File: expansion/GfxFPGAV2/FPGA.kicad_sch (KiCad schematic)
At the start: 31 parts, among them J1 JTAG, U1 XC6SLX9-FTG256, U301 XC3S500E-4PQG208I, U302 W25Q64JVSSIM, Y1 ECS-3963

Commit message: More work on VGA card
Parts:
- removed U1: XC6SLX9-FTG256, symbol FPGA_Xilinx_Spartan6:XC6SLX9-FTG256
- removed U301: XC3S500E-4PQG208I, Ddraig:QFP50P3060X3060X409-208N, symbol Ddraig:XC3S500E-4PQG208I
- added U2: XC6SLX9-FTG256, Package_BGA:Xilinx_FTG256, symbol Ddraig:XC6SLX9-FTG256
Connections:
- net +1V2: now also U2.G7 (VCCINT), U2.G9 (VCCINT), U2.H10 (VCCINT), U2.H8 (VCCINT), U2.J7 (VCCINT), U2.J9 (VCCINT), U2.K10 (VCCINT), U2.K8 (VCCINT)
- net +3V3: now also U2.B13 (VCCO_0), U2.B4 (VCCO_0), U2.B9 (VCCO_0), U2.D10 (VCCO_0), U2.D15 (VCCO_1), U2.D2 (VCCO_3), U2.D7 (VCCO_0), U2.E5 (VCCAUX), U2.F11 (VCCAUX), U2.F8 (VCCAUX), U2.G10 (VCCAUX), U2.G13 (VCCO_1), U2.G4 (VCCO_3), U2.H6 (VCCAUX), U2.J10 (VCCAUX), U2.J15 (VCCO_1), U2.J2 (VCCO_3), U2.K13 (VCCO_1), U2.K4 (VCCO_3), U2.L6 (VCCAUX), U2.L9 (VCCAUX), U2.N10 (VCCO_2), U2.N15 (VCCO_1), U2.N2 (VCCO_3), U2.N7 (VCCO_2), U2.R13 (VCCO_1), U2.R4 (VCCO_2), U2.R8 (VCCO_2)
- net FPGA_DONE: now also U2.P13 (DONE_2)
- net FPGA_PROGB: now also U2.T2 (PROGRAM_B_2)
- net GND: now also U2.A1 (GND), U2.A16 (GND), U2.B11 (GND), U2.B7 (GND), U2.D13 (GND), U2.D4 (GND), U2.E9 (GND), U2.G15 (GND), U2.G2 (GND), U2.G8 (GND), U2.H12 (GND), U2.H7 (GND), U2.H9 (GND), U2.J5 (GND), U2.J8 (GND), U2.K7 (GND), U2.K9 (GND), U2.L15 (GND), U2.L2 (GND), U2.M8 (GND), U2.N13 (GND), U2.P3 (GND), U2.R10 (GND), U2.R6 (GND), U2.T1 (GND), U2.T16 (GND)
- net R0: now also U2.A14 (IO_L65N_SCP2_0)
- net R1: now also U2.B14 (IO_L65P_SCP3_0)
- net R2: now also U2.B15 (IO_L29P_A23_M1A13_1)
- net R3: now also U2.B16 (IO_L29N_A22_M1A14_1)
- net TMS: now reaches J1.5 (Pin_5)
- net TMS: now also U2.A15 (TMS)
- net TDO: now reaches J1.4 (Pin_4)
- net TDO: now also U2.E14 (TDO)
- net TCK: now reaches J1.2 (Pin_2)
- net TCK: now also U2.C14 (TCK)
- net TDI: now reaches J1.3 (Pin_3)
- net TDI: now also U2.C12 (TDI)
- no-connect marks 18 -> 0
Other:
- moved on the sheet: C1, C301, C302, C303, C304, C305, C306, C307, C308, C309, C310, D1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

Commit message: Pinout done one VGA card
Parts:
- removed R10, R11, R9: 10K, Resistor_SMD:R_0805_2012Metric, symbol Device:R
- removed R3: 390R, Resistor_SMD:R_0805_2012Metric, symbol Device:R
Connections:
- net CLK_25MHZ is gone; now on net CLK_50MHZ: Y1.3 (O/P)
- net A1: now also U2.P9 (IO_L14N_D12_2); no longer R1.1
- net A10: now also U2.P5 (IO_L49N_D4_2)
- net A11: now also U2.R5 (IO_L48P_D7_2)
- net A12: now also U2.T5 (IO_L48N_RDWR_B_VREF_2)
- net A13: now also U2.N5 (IO_L49P_D3_2)
- net A14: now also U2.N4 (IO_L2N_3)
- net A15: now also U2.P4 (IO_L63P_2)
- net A16: now also U2.T4 (IO_L63N_2)
- net A17: now also U2.N3 (IO_L34P_M3UDQS_3)
- net A18: now also U2.M6 (IO_L64P_D8_2)
- net A19: now also U2.M5 (IO_L2P_3)
- net A2: now also U2.N8 (IO_L29N_GCLK2_2)
- net A3: now also U2.P8 (IO_L30P_GCLK1_D13_2)
- net A4: now also U2.T7 (IO_L32N_GCLK28_2)
- net A5: now also U2.R7 (IO_L32P_GCLK29_2)
- net A6: now also U2.P7 (IO_L31P_GCLK31_D14_2)
- net A7: now also U2.T6 (IO_L47N_2)
- net A8: now also U2.P6 (IO_L47P_2)
- net A9: now also U2.N6 (IO_L64N_D9_2)
- net B0: now also U2.H15 (IO_L37P_A7_M1A0_1)
- net B1: now also U2.H16 (IO_L37N_A6_M1A1_1)
- net B2: now also U2.J14 (IO_L43P_GCLK5_M1DQ4_1)
- net B3: now also U2.J16 (IO_L43N_GCLK4_M1DQ5_1)
- net B4: now also U2.K14 (IO_L41N_GCLK8_M1CASN_1)
- net B5: now also U2.K15 (IO_L44P_A3_M1DQ6_1)
- net B6: now also U2.K16 (IO_L44N_A2_M1DQ7_1)
- net B7: now also U2.L14 (IO_L47P_FWE_B_M1DQ0_1)
- net D0: now also U2.N14 (IO_L45P_A1_M1LDQS_1), U2.T14 (IO_L51P_M1DQ12_1)
- net D1: now also U2.R14 (IO_L50P_M1UDQS_1)
- net D10: now also R1.1, U2.N11 (IO_L13P_M1_2)
- net D11: now also U2.M10 (IO_L16N_VREF_2)
- net D12: now also U2.M12 (IO_L2P_CMPCLK_2)
- net D13: now also U2.N9 (IO_L14P_D11_2)
- net D14: now also U2.T9 (IO_L23N_2); no longer U302.2 (DO/IO1)
- net D15: now also U2.R9 (IO_L23P_2); no longer R4.2
- net D2: now also U2.T13 (IO_L51N_M1DQ13_1)
- net D3: now also U2.T12 (IO_L52N_M1DQ15_1)
- net D4: now also U2.R12 (IO_L52P_M1DQ14_1)
- net D5: now also U2.P12 (IO_L12N_D2_MISO3_2)
- net D6: now also U2.N12 (IO_L12P_D1_MISO2_2)
- net D7: now also R4.2, U2.T11 (IO_L1N_M0_CMPMISO_2)
- net D8: now also U2.M11 (IO_L2N_CMPMOSI_2)
- net D9: now also U2.P11 (IO_L13N_D10_2)
- net DATA_DIR: now also U2.R16 (IO_L49N_M1DQ11_1)
- net FLASH_CLK: now also U2.R11 (IO_L1P_CCLK_2)
- net FLASH_DI: now also U2.T10 (IO_L3N_MOSI_CSI_B_MISO0_2)
- net FPGA_INITB: now also U2.R3 (IO_L65P_INIT_B_2)
- net G0: now also U2.D12 (IO_L66N_SCP0_0)
- net G1: now also U2.E13 (IO_L1P_A25_1)
- net G2: now also U2.E15 (IO_L34P_A13_M1WE_1)
- net G3: now also U2.E16 (IO_L34N_A12_M1BA2_1)
- net G4: now also U2.F13 (IO_L32P_A17_M1A8_1)
- net G5: now also U2.F14 (IO_L32N_A16_M1A9_1)
- net G6: now also U2.F15 (IO_L35P_A11_M1A7_1)
- net G7: now also U2.F16 (IO_L35N_A10_M1A2_1)
- net GND: now also U2.P14 (SUSPEND)
- net HOST_CLK: now also U2.M7 (IO_L31N_GCLK30_D15_2)
- net HSYNC: now also U2.M14 (IO_L74N_DOUT_BUSY_1)
- net PIXELCLOCK: now also U2.M15 (IO_L46P_FCS_B_M1DQ2_1)
- net R4: now also U2.C13 (IO_L63P_SCP7_0)
- net R5: now also U2.C15 (IO_L33P_A15_M1A10_1)
- net R6: now also U2.C16 (IO_L33N_A14_M1A4_1)
- net R7: now also U2.D14 (IO_L31P_A19_M1CKE_1)
- net R~{W}: now also U2.P2 (IO_L33P_M3DQ12_3)
- net SRAM_A0: now also U2.A3 (IO_L83N_VREF_3)
- net SRAM_A1: now also U2.A2 (IO_L52N_M3A9_3)
- net SRAM_A10: now also U2.C11 (IO_L39P_0)
- net SRAM_A11: now also U2.A11 (IO_L39N_0)
- net SRAM_A12: now also U2.B12 (IO_L62P_0)
- net SRAM_A13: now also U2.A12 (IO_L62N_VREF_0)
- net SRAM_A14: now also U2.A13 (IO_L63N_SCP6_0)
- net SRAM_A15: now also U2.D9 (IO_L40N_0)
- net SRAM_A16: now also U2.A8 (IO_L33N_0)
- net SRAM_A17: now also U2.B8 (IO_L33P_0)
- net SRAM_A18: now also U2.C8 (IO_L38N_VREF_0)
- net SRAM_A19: now also U2.D8 (IO_L38P_0)
- net SRAM_A2: now also U2.B3 (IO_L83P_3)
- net SRAM_A3: now also U2.B2 (IO_L52P_M3A8_3)
- net SRAM_A4: now also U2.B1 (IO_L50N_M3BA2_3)
- net SRAM_A5: now also U2.H4 (IO_L44P_GCLK21_M3A5_3)
- net SRAM_A6: now also U2.H5 (IO_L43N_GCLK22_IRDY2_M3CASN_3)
- net SRAM_A7: now also U2.J3 (IO_L38P_M3DQ2_3)
- net SRAM_A8: now also U2.J4 (IO_L42N_GCLK24_M3LDM_3)
- net SRAM_A9: now also U2.D11 (IO_L66P_SCP1_0)
- net SRAM_D0: now also U2.E1 (IO_L46N_M3CLKN_3)
- net SRAM_D1: now also U2.E2 (IO_L46P_M3CLK_3)
- net SRAM_D10: now also U2.L5 (IO_L45N_M3ODT_3)
- net SRAM_D11: now also U2.L4 (IO_L45P_M3A3_3)
- net SRAM_D12: now also U2.L3 (IO_L36P_M3DQ8_3)
- net SRAM_D13: now also U2.L1 (IO_L36N_M3DQ9_3)
- net SRAM_D14: now also U2.K5 (IO_L47P_M3A0_3)
- net SRAM_D15: now also U2.K3 (IO_L42P_GCLK25_TRDY2_M3UDM_3)
- net SRAM_D16: now also U2.C4 (IO_L1P_HSWAPEN_0)
- net SRAM_D17: now also U2.A4 (IO_L1N_VREF_0)
- net SRAM_D18: now also U2.D5 (IO_L3P_0)
- net SRAM_D19: now also U2.C5 (IO_L3N_0)
- net SRAM_D2: now also U2.E3 (IO_L54N_M3A11_3)
- net SRAM_D20: now also U2.B5 (IO_L2P_0)
- net SRAM_D21: now also U2.A5 (IO_L2N_0)
- net SRAM_D22: now also U2.D6 (IO_L7P_0)
- net SRAM_D23: now also U2.C6 (IO_L7N_0)
- net SRAM_D24: now also U2.A10 (IO_L35N_GCLK16_0)
- net SRAM_D25: now also U2.B10 (IO_L35P_GCLK17_0)
- net SRAM_D26: now also U2.C10 (IO_L37N_GCLK12_0)
- net SRAM_D27: now also U2.E10 (IO_L37P_GCLK13_0)
- net SRAM_D28: now also U2.G1 (IO_L40N_M3DQ7_3)
- net SRAM_D29: now also U2.G3 (IO_L40P_M3DQ6_3)
- net SRAM_D3: now also U2.E4 (IO_L54P_M3RESET_3)
- net SRAM_D30: now also U2.G5 (IO_L51N_M3A4_3)
- net SRAM_D31: now also U2.G6 (IO_L51P_M3A10_3)
- net SRAM_D4: now also U2.F3 (IO_L53N_M3A12_3)
- net SRAM_D5: now also U2.F4 (IO_L53P_M3CKE_3)
- net SRAM_D6: now also U2.F5 (IO_L55N_M3A14_3)
- net SRAM_D7: now also U2.F6 (IO_L55P_M3A13_3)
- net SRAM_D8: now also U2.M2 (IO_L35P_M3DQ10_3)
- net SRAM_D9: now also U2.M1 (IO_L35N_M3DQ11_3)
- net VSYNC: now also U2.M13 (IO_L74P_AWAKE_1)
- net ~{ACCESS_LED}: now also U2.R1 (IO_L32N_M3DQ15_3)
- net ~{AS}: now also U2.R2 (IO_L32P_M3DQ14_3)
- net ~{BLANK}: now also U2.G14 (IO_L36P_A9_M1BA0_1)
- net ~{BUSEN}: now also U2.M9 (IO_L29P_GCLK3_2)
- net ~{CPU_DATAEN}: now also U2.P16 (IO_L48N_M1DQ9_1)
- net ~{CPU_DTACK}: now also U2.P1 (IO_L33N_M3DQ13_3)
- net ~{CPU_IRQ}: now also U2.N1 (IO_L34N_M3UDQSN_3)
- net ~{DATACS}: now also U2.A7 (IO_L6N_0)
- net ~{FLASH_CS}: now also U2.T3 (IO_L65N_CSO_B_2)
- net ~{LDS}: now also U2.M3 (IO_L1N_VREF_3)
- net ~{REGCS}: now also U2.C2 (IO_L48N_M3BA1_3)
- net ~{RESET}: now also U2.J1 (IO_L38N_M3DQ3_3)
- net ~{SRAM_CS}: now also U2.C3 (IO_L48P_M3BA0_3)
- net ~{SRAM_LB0}: now also U2.K2 (IO_L37P_M3DQ0_3)
- net ~{SRAM_LB1}: now also U2.H2 (IO_L39P_M3LDQS_3)
- net ~{SRAM_UB0}: now also U2.K1 (IO_L37N_M3DQ1_3)
- net ~{SRAM_UB1}: now also U2.H3 (IO_L44N_GCLK20_M3A6_3)
- net ~{SRAM_WE}: now also U2.C7 (IO_L6P_0)
- net ~{UDS}: now also U2.M4 (IO_L1P_3)
- net FLASH_DO: now reaches U2.P10 (IO_L3P_D0_DIN_MISO_MISO1_2)
- net FLASH_DO: now also U302.2 (DO/IO1)
- net CLK_50MHZ: now reaches U2.T8 (IO_L30N_GCLK0_USERCCLK_2)
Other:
- moved on the sheet: C301, C302, C303, C304, C305, C306, C307, C308, C309, C310, R4

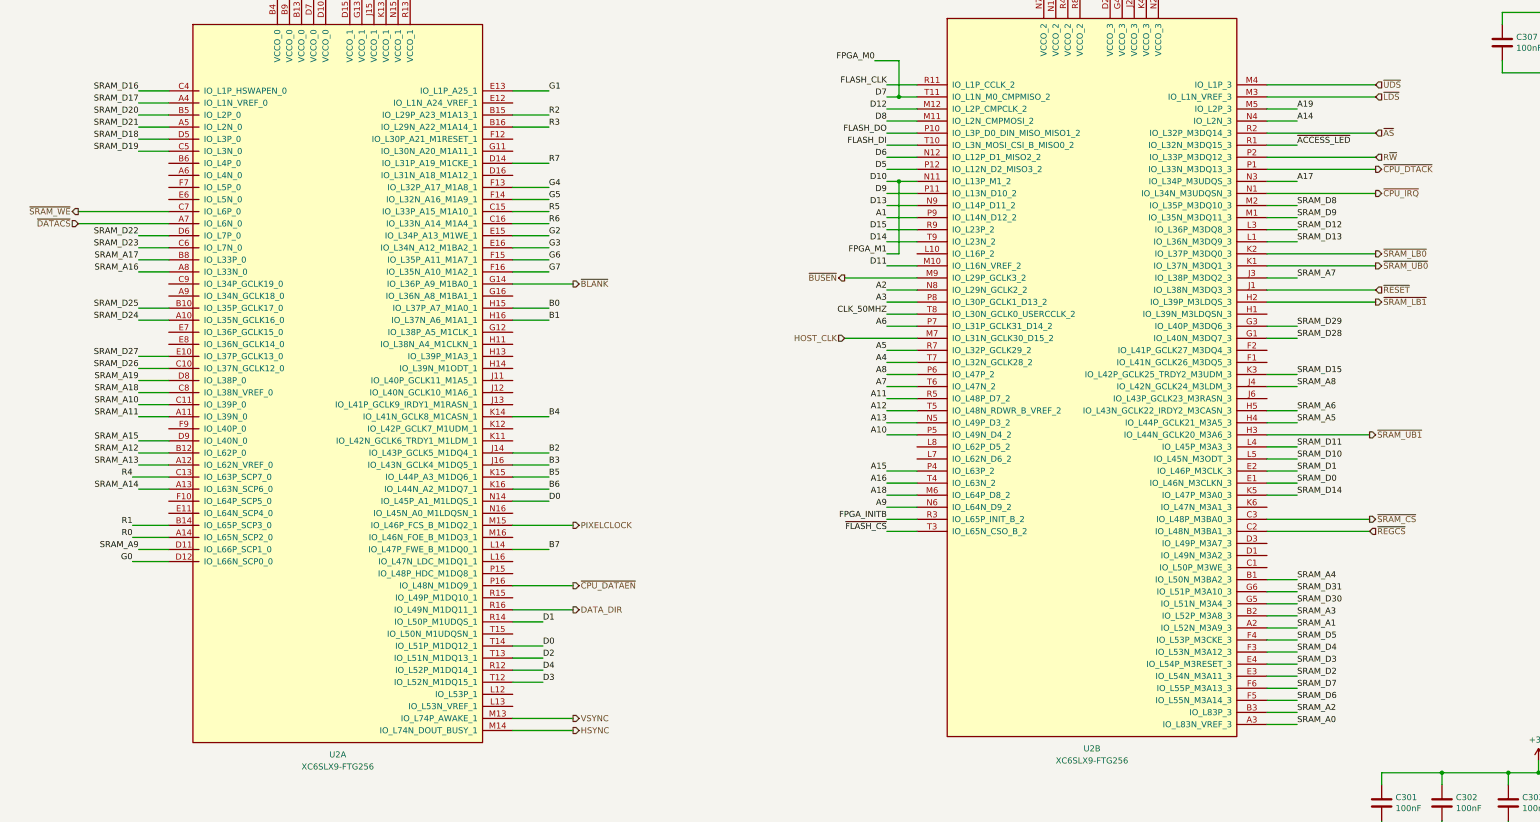
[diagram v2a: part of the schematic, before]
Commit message: intitial FPGA routing done
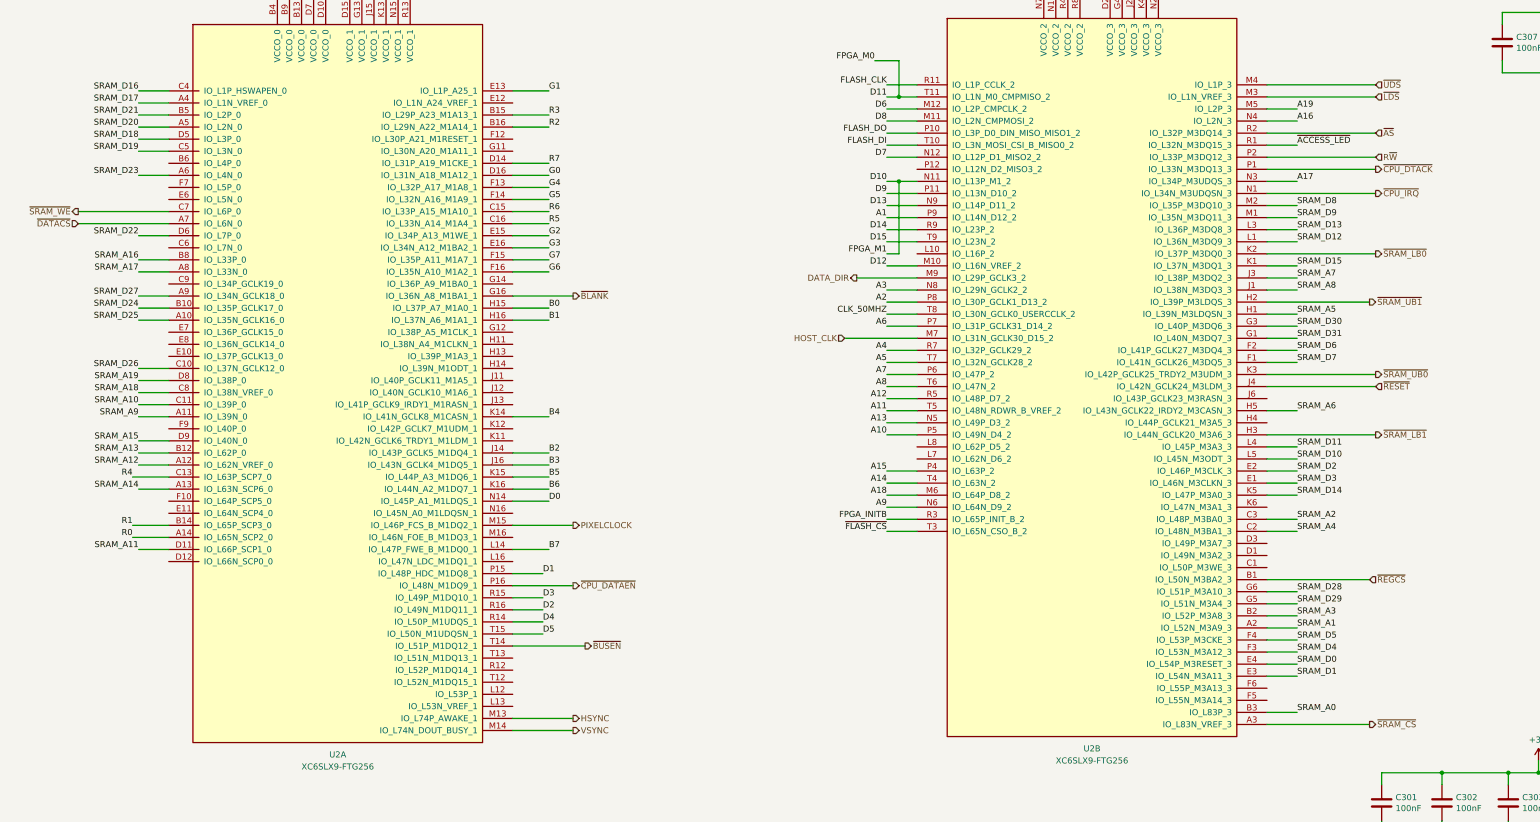
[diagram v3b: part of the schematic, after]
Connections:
- net A11: now also U2.T5 (IO_L48N_RDWR_B_VREF_2); no longer U2.R5 (IO_L48P_D7_2)
- net A12: now also U2.R5 (IO_L48P_D7_2); no longer U2.T5 (IO_L48N_RDWR_B_VREF_2)
- net A14: now also U2.T4 (IO_L63N_2); no longer U2.N4 (IO_L2N_3)
- net A16: now also U2.N4 (IO_L2N_3); no longer U2.T4 (IO_L63N_2)
- net A2: now also U2.P8 (IO_L30P_GCLK1_D13_2); no longer U2.N8 (IO_L29N_GCLK2_2)
- net A3: now also U2.N8 (IO_L29N_GCLK2_2); no longer U2.P8 (IO_L30P_GCLK1_D13_2)
- net A4: now also U2.R7 (IO_L32P_GCLK29_2); no longer U2.T7 (IO_L32N_GCLK28_2)
- net A5: now also U2.T7 (IO_L32N_GCLK28_2); no longer U2.R7 (IO_L32P_GCLK29_2)
- net A7: now also U2.P6 (IO_L47P_2); no longer U2.T6 (IO_L47N_2)
- net A8: now also U2.T6 (IO_L47N_2); no longer U2.P6 (IO_L47P_2)
- net D0: no longer U2.T14 (IO_L51P_M1DQ12_1)
- net D1: now also U2.P15 (IO_L48P_HDC_M1DQ8_1); no longer U2.R14 (IO_L50P_M1UDQS_1)
- net D11: now also R4.2, U2.T11 (IO_L1N_M0_CMPMISO_2); no longer U2.M10 (IO_L16N_VREF_2)
- net D12: now also U2.M10 (IO_L16N_VREF_2); no longer U2.M12 (IO_L2P_CMPCLK_2)
- net D14: now also U2.R9 (IO_L23P_2); no longer U2.T9 (IO_L23N_2)
- net D15: now also U2.T9 (IO_L23N_2); no longer U2.R9 (IO_L23P_2)
- net D2: now also U2.R16 (IO_L49N_M1DQ11_1); no longer U2.T13 (IO_L51N_M1DQ13_1)
- net D3: now also U2.R15 (IO_L49P_M1DQ10_1); no longer U2.T12 (IO_L52N_M1DQ15_1)
- net D4: now also U2.R14 (IO_L50P_M1UDQS_1); no longer U2.R12 (IO_L52P_M1DQ14_1)
- net D5: now also U2.T15 (IO_L50N_M1UDQSN_1); no longer U2.P12 (IO_L12N_D2_MISO3_2)
- net D6: now also U2.M12 (IO_L2P_CMPCLK_2); no longer U2.N12 (IO_L12P_D1_MISO2_2)
- net D7: now also U2.N12 (IO_L12P_D1_MISO2_2); no longer R4.2, U2.T11 (IO_L1N_M0_CMPMISO_2)
- net DATA_DIR: now also U2.M9 (IO_L29P_GCLK3_2); no longer U2.R16 (IO_L49N_M1DQ11_1)
- net G0: now also U2.D16 (IO_L31N_A18_M1A12_1); no longer U2.D12 (IO_L66N_SCP0_0)
- net G6: now also U2.F16 (IO_L35N_A10_M1A2_1); no longer U2.F15 (IO_L35P_A11_M1A7_1)
- net G7: now also U2.F15 (IO_L35P_A11_M1A7_1); no longer U2.F16 (IO_L35N_A10_M1A2_1)
- net HSYNC: now also U2.M13 (IO_L74P_AWAKE_1); no longer U2.M14 (IO_L74N_DOUT_BUSY_1)
- net R2: now also U2.B16 (IO_L29N_A22_M1A14_1); no longer U2.B15 (IO_L29P_A23_M1A13_1)
- net R3: now also U2.B15 (IO_L29P_A23_M1A13_1); no longer U2.B16 (IO_L29N_A22_M1A14_1)
- net R5: now also U2.C16 (IO_L33N_A14_M1A4_1); no longer U2.C15 (IO_L33P_A15_M1A10_1)
- net R6: now also U2.C15 (IO_L33P_A15_M1A10_1); no longer U2.C16 (IO_L33N_A14_M1A4_1)
- net SRAM_A0: now also U2.B3 (IO_L83P_3); no longer U2.A3 (IO_L83N_VREF_3)
- net SRAM_A11: now also U2.D11 (IO_L66P_SCP1_0); no longer U2.A11 (IO_L39N_0)
- net SRAM_A12: now also U2.A12 (IO_L62N_VREF_0); no longer U2.B12 (IO_L62P_0)
- net SRAM_A13: now also U2.B12 (IO_L62P_0); no longer U2.A12 (IO_L62N_VREF_0)
- net SRAM_A16: now also U2.B8 (IO_L33P_0); no longer U2.A8 (IO_L33N_0)
- net SRAM_A17: now also U2.A8 (IO_L33N_0); no longer U2.B8 (IO_L33P_0)
- net SRAM_A2: now also U2.C3 (IO_L48P_M3BA0_3); no longer U2.B3 (IO_L83P_3)
- net SRAM_A4: now also U2.C2 (IO_L48N_M3BA1_3); no longer U2.B1 (IO_L50N_M3BA2_3)
- net SRAM_A5: now also U2.H1 (IO_L39N_M3LDQSN_3); no longer U2.H4 (IO_L44P_GCLK21_M3A5_3)
- net SRAM_A8: now also U2.J1 (IO_L38N_M3DQ3_3); no longer U2.J4 (IO_L42N_GCLK24_M3LDM_3)
- net SRAM_A9: now also U2.A11 (IO_L39N_0); no longer U2.D11 (IO_L66P_SCP1_0)
- net SRAM_D0: now also U2.E4 (IO_L54P_M3RESET_3); no longer U2.E1 (IO_L46N_M3CLKN_3)
- net SRAM_D1: now also U2.E3 (IO_L54N_M3A11_3); no longer U2.E2 (IO_L46P_M3CLK_3)
- net SRAM_D12: now also U2.L1 (IO_L36N_M3DQ9_3); no longer U2.L3 (IO_L36P_M3DQ8_3)
- net SRAM_D13: now also U2.L3 (IO_L36P_M3DQ8_3); no longer U2.L1 (IO_L36N_M3DQ9_3)
- net SRAM_D15: now also U2.K1 (IO_L37N_M3DQ1_3); no longer U2.K3 (IO_L42P_GCLK25_TRDY2_M3UDM_3)
- net SRAM_D2: now also U2.E2 (IO_L46P_M3CLK_3); no longer U2.E3 (IO_L54N_M3A11_3)
- net SRAM_D20: now also U2.A5 (IO_L2N_0); no longer U2.B5 (IO_L2P_0)
- net SRAM_D21: now also U2.B5 (IO_L2P_0); no longer U2.A5 (IO_L2N_0)
- net SRAM_D23: now also U2.A6 (IO_L4N_0); no longer U2.C6 (IO_L7N_0)
- net SRAM_D24: now also U2.B10 (IO_L35P_GCLK17_0); no longer U2.A10 (IO_L35N_GCLK16_0)
- net SRAM_D25: now also U2.A10 (IO_L35N_GCLK16_0); no longer U2.B10 (IO_L35P_GCLK17_0)
- net SRAM_D27: now also U2.A9 (IO_L34N_GCLK18_0); no longer U2.E10 (IO_L37P_GCLK13_0)
- net SRAM_D28: now also U2.G6 (IO_L51P_M3A10_3); no longer U2.G1 (IO_L40N_M3DQ7_3)
- net SRAM_D29: now also U2.G5 (IO_L51N_M3A4_3); no longer U2.G3 (IO_L40P_M3DQ6_3)
- net SRAM_D3: now also U2.E1 (IO_L46N_M3CLKN_3); no longer U2.E4 (IO_L54P_M3RESET_3)
- net SRAM_D30: now also U2.G3 (IO_L40P_M3DQ6_3); no longer U2.G5 (IO_L51N_M3A4_3)
- net SRAM_D31: now also U2.G1 (IO_L40N_M3DQ7_3); no longer U2.G6 (IO_L51P_M3A10_3)
- net SRAM_D6: now also U2.F2 (IO_L41P_GCLK27_M3DQ4_3); no longer U2.F5 (IO_L55N_M3A14_3)
- net SRAM_D7: now also U2.F1 (IO_L41N_GCLK26_M3DQ5_3); no longer U2.F6 (IO_L55P_M3A13_3)
- net VSYNC: now also U2.M14 (IO_L74N_DOUT_BUSY_1); no longer U2.M13 (IO_L74P_AWAKE_1)
- net ~{BLANK}: now also U2.G16 (IO_L36N_A8_M1BA1_1); no longer U2.G14 (IO_L36P_A9_M1BA0_1)
- net ~{BUSEN}: now also U2.T14 (IO_L51P_M1DQ12_1); no longer U2.M9 (IO_L29P_GCLK3_2)
- net ~{REGCS}: now also U2.B1 (IO_L50N_M3BA2_3); no longer U2.C2 (IO_L48N_M3BA1_3)
- net ~{RESET}: now also U2.J4 (IO_L42N_GCLK24_M3LDM_3); no longer U2.J1 (IO_L38N_M3DQ3_3)
- net ~{SRAM_CS}: now also U2.A3 (IO_L83N_VREF_3); no longer U2.C3 (IO_L48P_M3BA0_3)
- net ~{SRAM_LB1}: now also U2.H3 (IO_L44N_GCLK20_M3A6_3); no longer U2.H2 (IO_L39P_M3LDQS_3)
- net ~{SRAM_UB0}: now also U2.K3 (IO_L42P_GCLK25_TRDY2_M3UDM_3); no longer U2.K1 (IO_L37N_M3DQ1_3)
- net ~{SRAM_UB1}: now also U2.H2 (IO_L39P_M3LDQS_3); no longer U2.H3 (IO_L44N_GCLK20_M3A6_3)
